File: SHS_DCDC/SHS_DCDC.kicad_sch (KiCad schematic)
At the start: 23 parts, among them J1 Barrel_Jack, Q1 BSS84, Q14 PMV100XPEAR, Q15 BSS84, Q16 PMV100XPEAR, U1 RT8299-WDFN10L

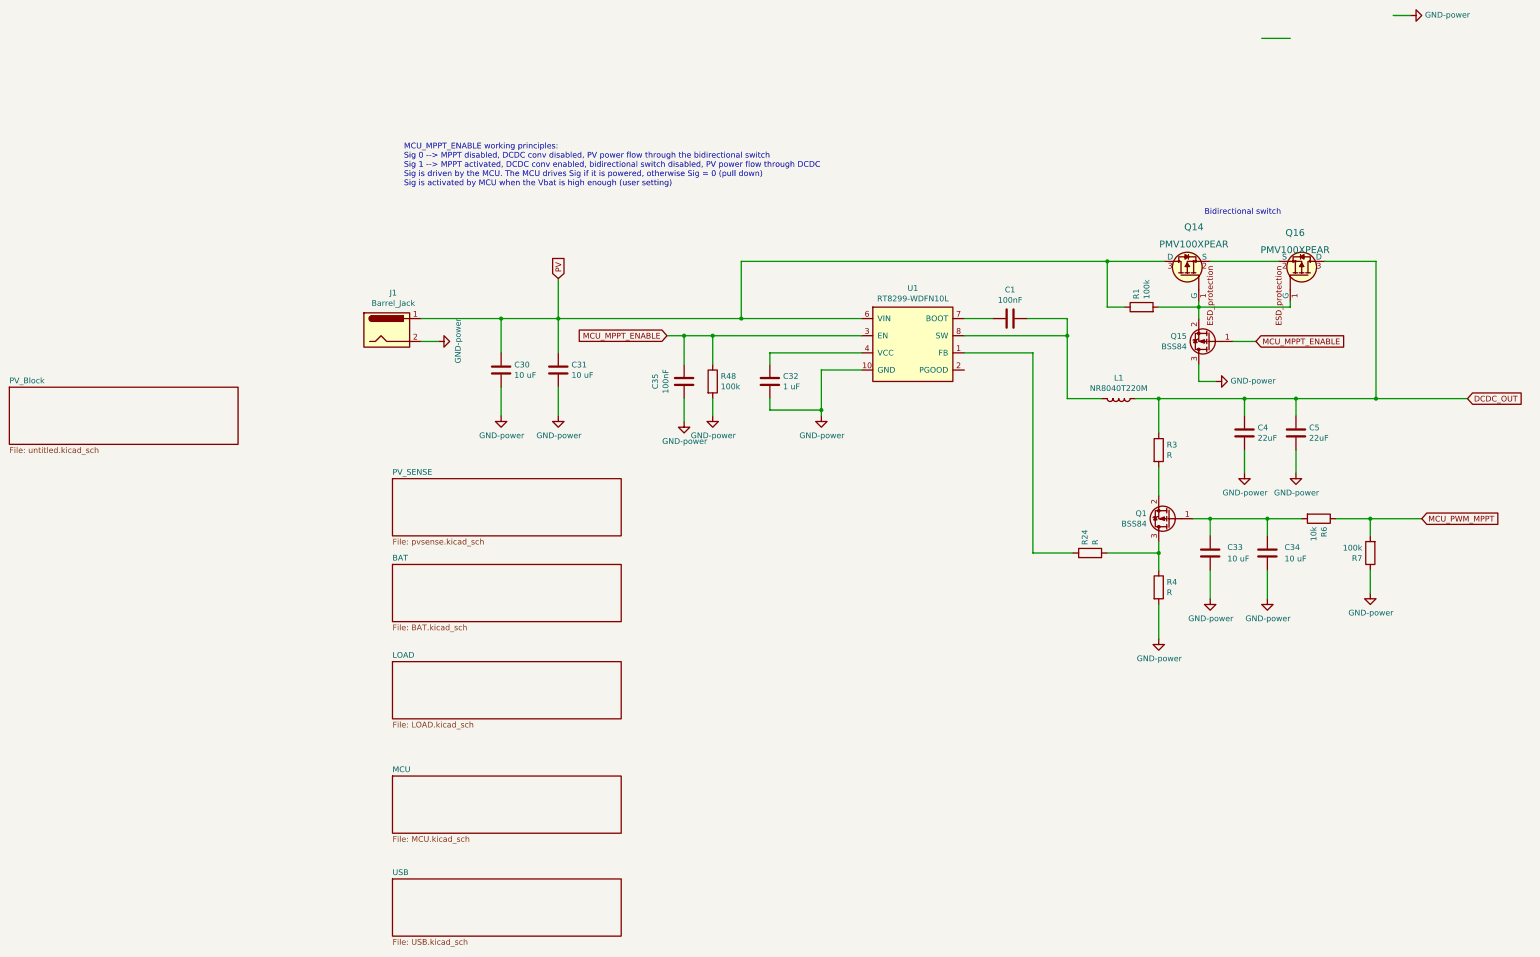
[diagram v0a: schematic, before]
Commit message: ADC_PV & BAT
Blocks related to ADC reading of PV and BAT added on the physical board.
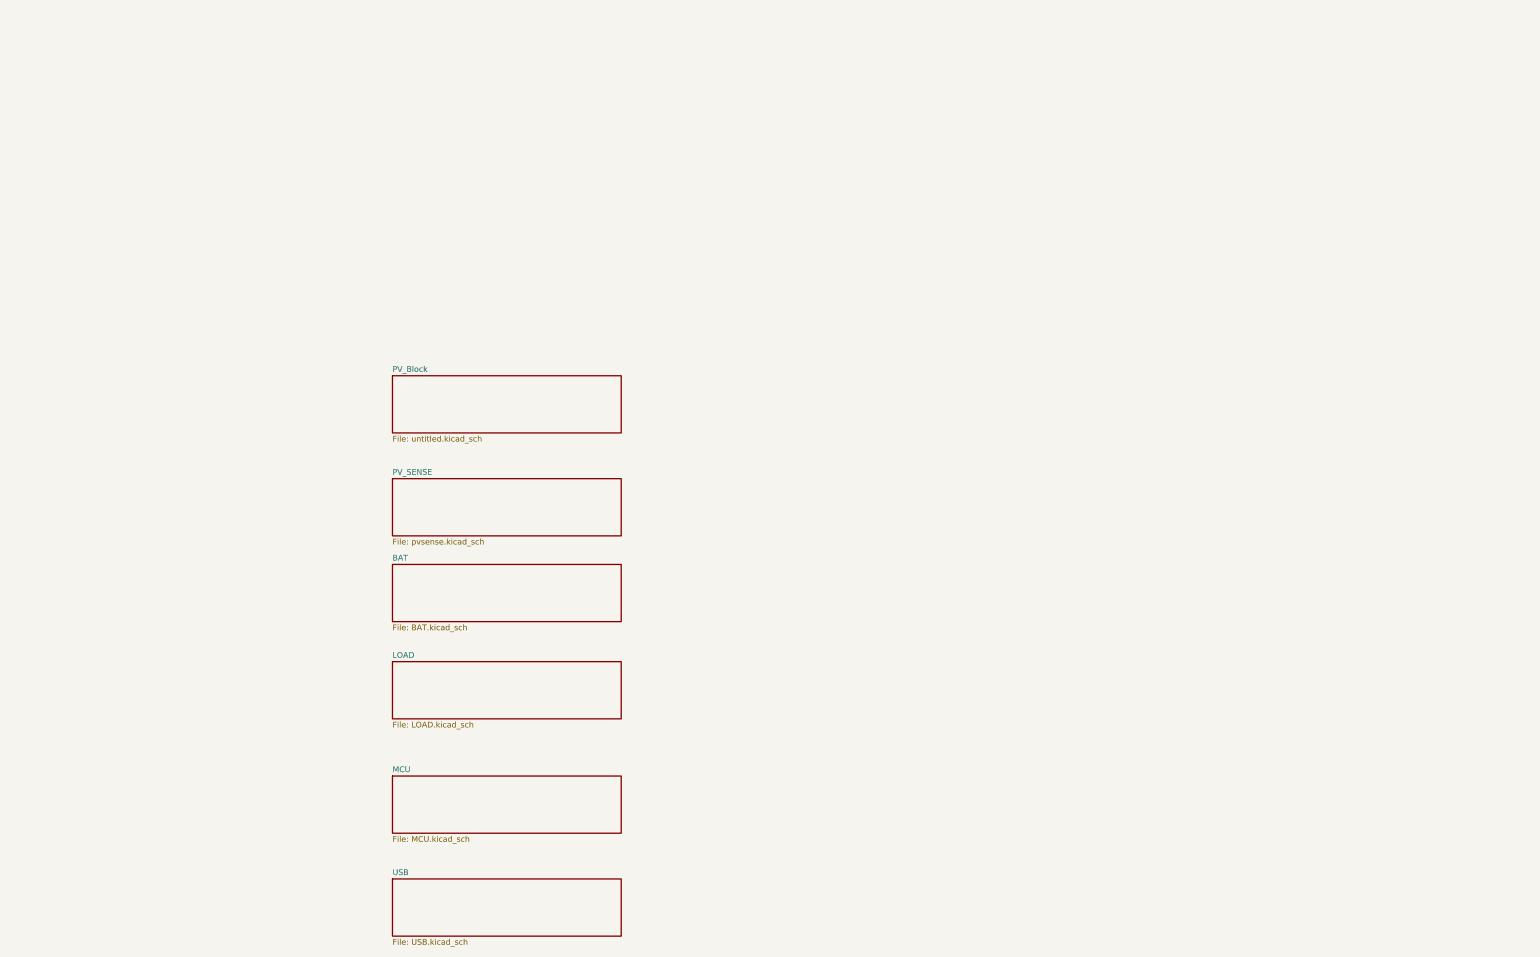
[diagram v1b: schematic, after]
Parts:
- removed C1, C35: 100nF, Capacitor_SMD:C_0402_1005Metric, symbol SHS_DCDC:C-Device
- removed C30, C31: 10 uF, Capacitor_SMD:C_0805_2012Metric, symbol SHS_DCDC:C-Device
- removed C32: 1 uF, Capacitor_SMD:C_0402_1005Metric, symbol SHS_DCDC:C-Device
- removed C33, C34: 10 uF, Capacitor_SMD:C_0603_1608Metric, symbol Device:C
- removed C4, C5: 22uF, Capacitor_SMD:C_0805_2012Metric, symbol SHS_DCDC:C-Device
- removed J1: Barrel_Jack, digikey-footprints:Barrel_Jack_5.5mmODx2.1mmID_PJ-202A, symbol SHS_DCDC:Barrel_Jack-Connector
- removed L1: NR8040T220M, Inductor_SMD:L_Taiyo-Yuden_NR-80xx, symbol SHS_DCDC:L-Device
- removed Q1, Q15: BSS84, Package_TO_SOT_SMD:SOT-23, symbol SHS_DCDC:BSS84-Transistor_FET
- removed Q14, Q16: PMV100XPEAR, digikey-kicad-library-master:SOT-23-3, symbol SHS_DCDC:PMV100XPEAR
- removed R1: 100k, Resistor_SMD:R_0402_1005Metric, symbol SHS_DCDC:R-Device
- removed R24, R3, R4: R, Resistor_SMD:R_0603_1608Metric, symbol SHS_DCDC:R-Device
- removed R48, R7: 100k, Resistor_SMD:R_0603_1608Metric, symbol SHS_DCDC:R-Device
- removed R6: 10k, Resistor_SMD:R_0603_1608Metric, symbol SHS_DCDC:R-Device
- removed U1: RT8299-WDFN10L, Library:RT8299-WDFN, symbol SHS_DCDC:RT8299-WDFN10L
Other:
- note removed: "Bidirectional switch"
- note removed: "MCU_MPPT_ENABLE working principles: Sig 0 --> MPPT disabled, DCDC conv disabled, PV power flow through the bidirectional switch Sig 1 --> MPPT activated, DCDC conv enabled, bidirectional switch disabled, PV power flow through DCDC Sig is driven by the MCU. The MCU drives Sig if it is powered, otherwise Sig = 0 (pull down) Sig is activated by MCU when the Vbat is high enough (user setting)"
